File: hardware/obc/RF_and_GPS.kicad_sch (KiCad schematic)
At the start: 15 parts, among them J602 SMA RA Connector, J603 SMA RA Connector, J604 SMA RA Connector, U102 BMI088, U601 RFM98PW, U602 S1216V8, U603 GP2S1+

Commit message: obc: Fixed errors from design review
- Gave proper attribution on all pages
- Spread out components on Avionics page
- Changed GPS power circuit
- Added a DNP resistor in between VBATT and VWATCHEDRAIL
- Added various other part numbers on Power Supervisor and Watch Dog Page
- Changed Power Supervisor and Watch Dog Page to page 3
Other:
- company: Ruchir Kavulli, Michael Lyle -> Ruchir Kavulli, Luke Titi, Michael Lyle
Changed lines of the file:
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@@
 		(date "2024-06-07")
 		(rev "1")
-		(company "Ruchir Kavulli, Michael Lyle")
+		(company "Ruchir Kavulli, Luke Titi, Michael Lyle")
 		(comment 1 "Derived from PyCubed Mainboard v5")
 	)

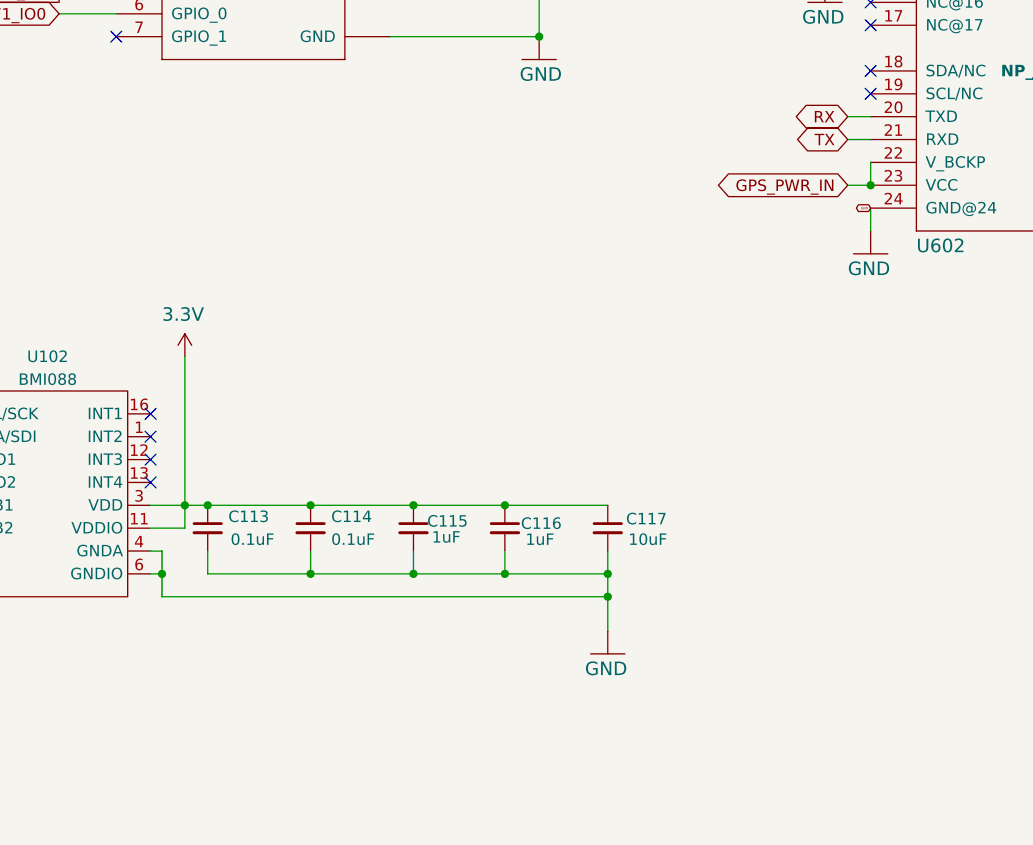
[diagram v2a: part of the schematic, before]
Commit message: obc: Fixed second design review, and fixed up BOM
- added layout comments on schematic
- fixed various comments
- added many LCSC # for components
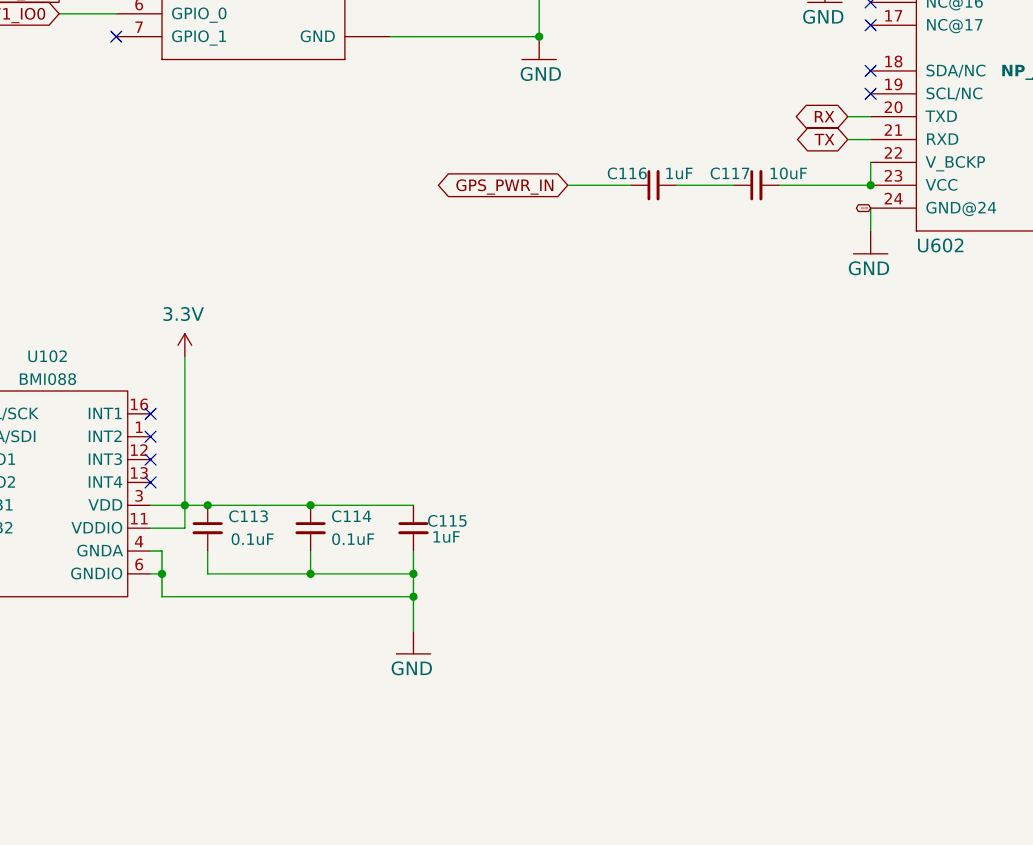
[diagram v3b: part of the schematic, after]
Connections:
- net 3.3V: no longer C116.1, C117.1
- net GND: no longer C116.2, C117.2
- net GPS_PWR_IN: now also C116.1; no longer U602.22 (V_BCKP), U602.23 (VCC)
- new net: C117.2, U602.22 (V_BCKP), U602.23 (VCC)
- new net: C116.2, C117.1
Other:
- moved on the sheet: C116, C117

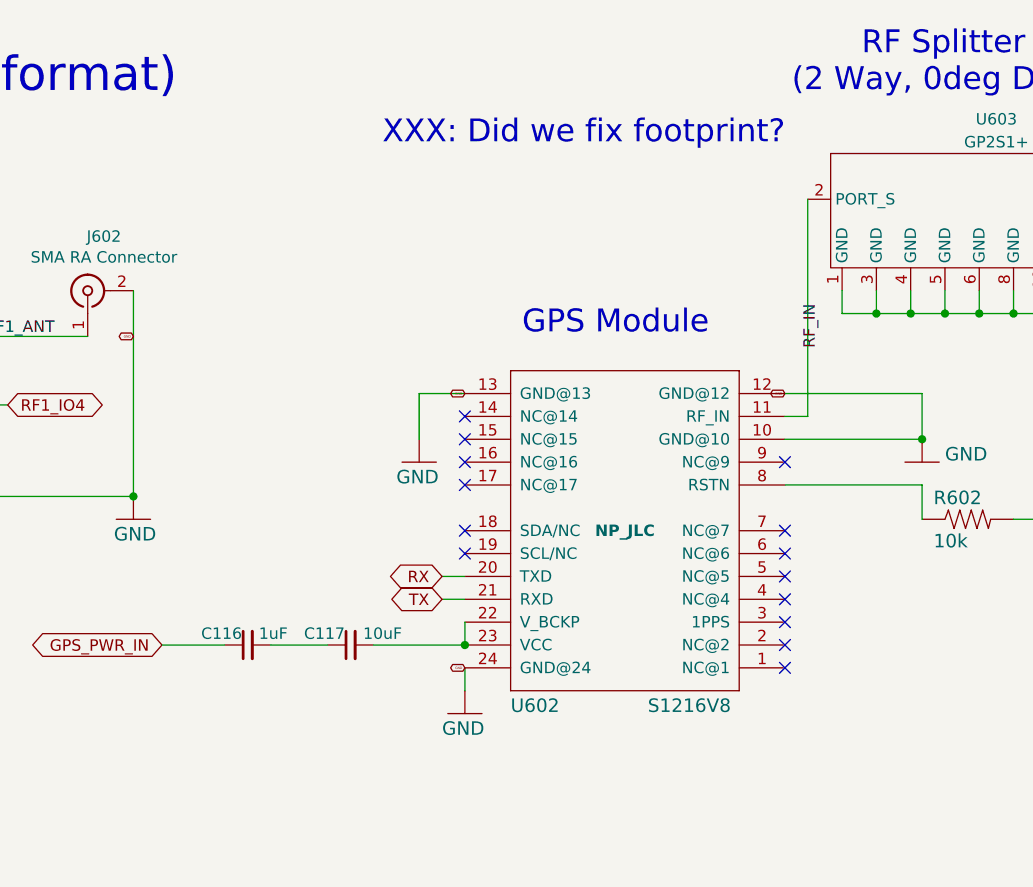
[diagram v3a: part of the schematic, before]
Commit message: obc: final cleanup before review
ex. cleaned wires in PCB, made text nicer on the schematic
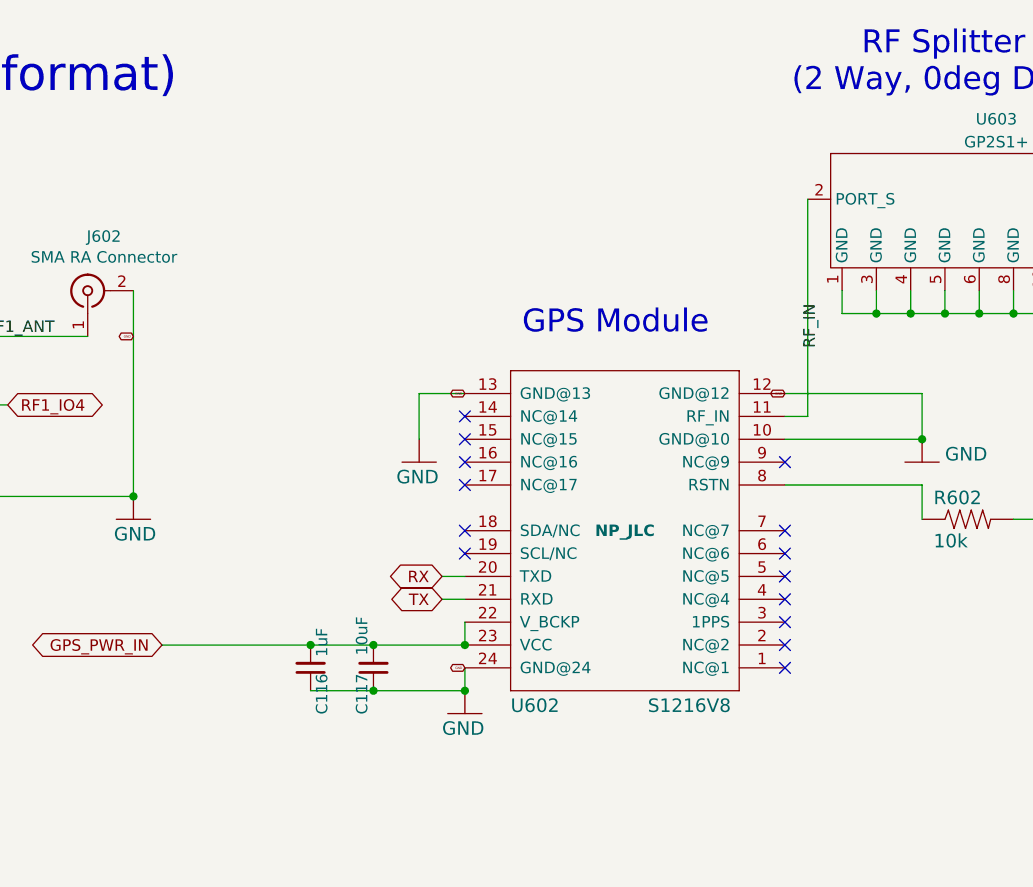
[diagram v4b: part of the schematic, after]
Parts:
- U102: LCSC (none) -> C194919
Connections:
- net GND: now also C116.1, C117.1
- net GPS_PWR_IN: now also C116.2, C117.2, U602.22 (V_BCKP), U602.23 (VCC); no longer C116.1
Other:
- note removed: "XXX: Did we fix footprint?"
- moved on the sheet: C116, C117
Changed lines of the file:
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@@
 	)
 	(junction
+		(at 154.94 97.79)
+		(diameter 0)
+		(color 0 0 0 0)
+	)
+	(junction
 		(at 231.14 55.88)
 		(diameter 0)
@@
 	)
 	(junction
+		(at 144.78 97.79)
+		(diameter 0)
+		(color 0 0 0 0)
+	)
+	(junction
+		(at 137.795 92.71)
+		(diameter 0)
+		(color 0 0 0 0)
+	)
+	(junction
 		(at 219.71 55.88)
 		(diameter 0)
@@
 	)
 	(junction
+		(at 144.78 92.71)
+		(diameter 0)
+		(color 0 0 0 0)
+	)
+	(junction
 		(at 81.28 128.27)
 		(diameter 0)
@@
 	(wire
 		(pts
+			(xy 137.795 97.79) (xy 144.78 97.79)
+		)
+		(stroke
+			(width 0)
+			(type default)
+		)
+	)
+	(wire
+		(pts
 			(xy 59.69 58.42) (xy 59.69 53.34)
 		)
@@
 	(wire
 		(pts
-			(xy 121.285 92.71) (xy 128.27 92.71)
+			(xy 121.285 92.71) (xy 137.795 92.71)
 		)
 		(stroke
@@
 	(wire
 		(pts
-			(xy 133.35 92.71) (xy 139.7 92.71)
-		)
-		(stroke
-			(width 0)
-			(type default)
-		)
-	)
-	(wire
-		(pts
 			(xy 205.74 69.85) (xy 190.5 69.85)
 		)
@@
 	(wire
 		(pts
+			(xy 137.795 92.71) (xy 144.78 92.71)
+		)
+		(stroke
+			(width 0)
+			(type default)
+		)
+	)
+	(wire
+		(pts
 			(xy 101.6 58.42) (xy 113.03 58.42)
 		)
@@
 	(wire
 		(pts
+			(xy 144.78 97.79) (xy 154.94 97.79)
+		)
+		(stroke
+			(width 0)
+			(type default)
+		)
+	)
+	(wire
+		(pts
 			(xy 154.94 87.63) (xy 152.4 87.63)
 		)
@@
 		)
 	)
-	(text "XXX: Did we fix footprint?"
-		(exclude_from_sim no)
-		(at 168.148 35.814 0)
-		(effects
-			(font
-				(size 2.54 2.54)
-			)
-		)
-	)
 	(label "RF_IN"
 		(at 194.31 59.69 90)
@@
 			)
 		)
+		(property "LCSC" "C194919"
+			(at 63.5 113.03 0)
+			(effects
+				(font
+					(size 1.27 1.27)
+				)
+				(hide yes)
+			)
+		)
 		(pin "9"
 		)
@@
 	(symbol
 		(lib_id "mainboard:C_Small")
-		(at 142.24 92.71 90)
+		(at 144.78 95.25 180)
 		(unit 1)
 		(exclude_from_sim no)
@@
 		(dnp no)
 		(property "Reference" "C117"
-			(at 141.605 91.44 90)
+			(at 143.51 95.885 90)
 			(effects
 				(font
@@
 		)
 		(property "Value" "10uF"
-			(at 147.955 91.44 90)
+			(at 143.51 89.535 90)
 			(effects
 				(font
@@
 		)
 		(property "Footprint" "Capacitor_SMD:C_0603_1608Metric"
-			(at 142.24 92.71 0)
+			(at 144.78 95.25 0)
 			(effects
 				(font
@@
 		)
 		(property "Datasheet" ""
-			(at 142.24 92.71 0)
+			(at 144.78 95.25 0)
 			(effects
 				(font
@@
 		)
 		(property "Description" "10V 10uF X5R ±20% 0603"
-			(at 142.24 92.71 0)
+			(at 144.78 95.25 0)
 			(effects
 				(font
@@
 		)
 		(property "LCSC" "C85713"
-			(at 142.24 92.71 0)
+			(at 144.78 95.25 0)
 			(effects
 				(font
@@
 		)
 		(property "Manufacturer_Name" " Samsung Electro-Mechanics"
-			(at 142.24 92.71 0)
+			(at 144.78 95.25 0)
 			(effects
 				(font
@@
 		)
 		(property "Manufacturer_Part_Number" "CL10A106MP8NNNC"
-			(at 142.24 92.71 0)
+			(at 144.78 95.25 0)
 			(effects
 				(font
@@
 		)
 		(property "Notes" "10V ok?"
-			(at 142.24 92.71 0)
+			(at 144.78 95.25 0)
 			(effects
 				(font
@@
 		)
 		(property "Height" ""
-			(at 142.24 92.71 0)
+			(at 144.78 95.25 0)
 			(effects
 				(font
@@
 		)
 		(property "Mouser Part Number" ""
-			(at 142.24 92.71 0)
+			(at 144.78 95.25 0)
 			(effects
 				(font
@@
 		)
 		(property "Mouser Price/Stock" ""
-			(at 142.24 92.71 0)
+			(at 144.78 95.25 0)
 			(effects
 				(font
@@
 		)
 		(property "Sim.Type" ""
-			(at 142.24 92.71 0)
+			(at 144.78 95.25 0)
 			(effects
 				(font
@@
 	(symbol
 		(lib_id "mainboard:C_Small")
-		(at 130.81 92.71 90)
+		(at 137.795 95.25 0)
+		(mirror x)
 		(unit 1)
 		(exclude_from_sim no)
@@
 		(dnp no)
 		(property "Reference" "C116"
-			(at 130.175 91.44 90)
+			(at 139.065 95.885 90)
 			(effects
 				(font
@@
 		)
 		(property "Value" "1uF"
-			(at 135.255 91.44 90)
+			(at 139.065 90.805 90)
 			(effects
 				(font
@@
 		)
 		(property "Footprint" "Capacitor_SMD:C_0603_1608Metric"
-			(at 130.81 92.71 0)
+			(at 137.795 95.25 0)
 			(effects
 				(font
@@
 		)
 		(property "Datasheet" ""
-			(at 130.81 92.71 0)
+			(at 137.795 95.25 0)
 			(effects
 				(font
@@
 		)
 		(property "Description" "16V 1uF X7R ±10% 0603"
-			(at 130.81 92.71 0)
+			(at 137.795 95.25 0)
 			(effects
 				(font
@@
 		)
 		(property "LCSC" "C59782"
-			(at 130.81 92.71 0)
+			(at 137.795 95.25 0)
 			(effects
 				(font
@@
 		)
 		(property "Notes" "16V ok?"
-			(at 130.81 92.71 0)
+			(at 137.795 95.25 0)
 			(effects
 				(font
@@
 		)
 		(property "Height" ""
-			(at 130.81 92.71 0)
+			(at 137.795 95.25 0)
 			(effects
 				(font
@@
 		)
 		(property "Mouser Part Number" ""
-			(at 130.81 92.71 0)
+			(at 137.795 95.25 0)
 			(effects
 				(font
@@
 		)
 		(property "Mouser Price/Stock" ""
-			(at 130.81 92.71 0)
+			(at 137.795 95.25 0)
 			(effects
 				(font
@@
 		)
 		(property "Manufacturer_Name" " Samsung Electro-Mechanics"
-			(at 130.81 92.71 0)
+			(at 137.795 95.25 0)
 			(effects
 				(font
@@
 		)
 		(property "Manufacturer_Part_Number" " CL10B105KO8NNNC"
-			(at 130.81 92.71 0)
+			(at 137.795 95.25 0)
 			(effects
 				(font
@@
 		)
 		(property "Sim.Type" ""
-			(at 130.81 92.71 0)
+			(at 137.795 95.25 0)
 			(effects
 				(font
